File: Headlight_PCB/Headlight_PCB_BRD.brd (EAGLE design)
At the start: 100 x 80 mm, 7 parts, among them Q1 NTD3055L104G, Q2 NTD3055L104G

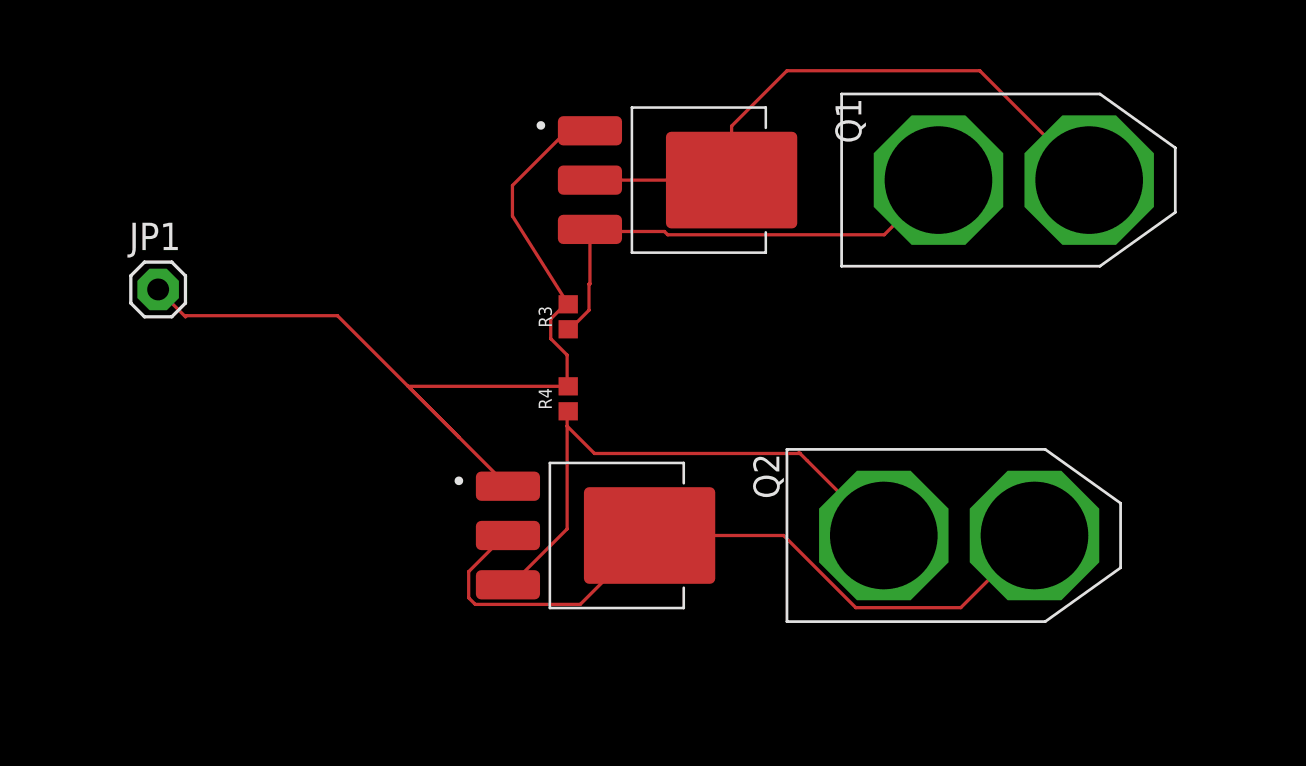
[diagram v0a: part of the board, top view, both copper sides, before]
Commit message: Updating\renaming Headlight_PCB files, adding pngs
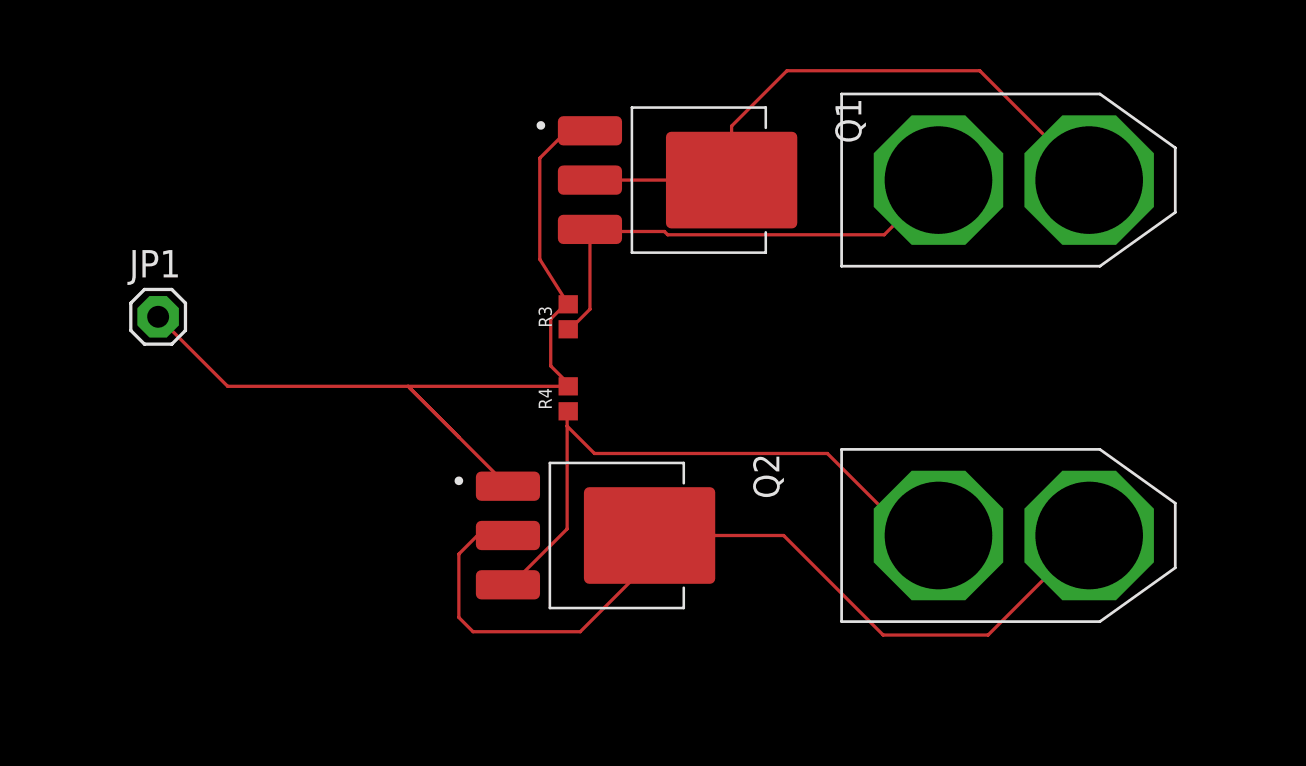
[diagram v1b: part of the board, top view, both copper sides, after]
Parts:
- moved U$2 2.54 mm to (40.6, 34.3)
- moved JP1 1.27 mm to (8.89, 44.5)
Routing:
- net N$4: track 34.2 -> 41.6 mm
- net N$5: track 26.4 -> 28.9 mm
- net N$7: track 46.3 -> 44.8 mm
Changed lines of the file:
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@@
 </autorouter>
 <elements>
-<element name="JP1" library="adafruit" package="1X01" value="" x="8.89" y="45.72" smashed="yes">
-<attribute name="NAME" x="7.5438" y="47.5488" size="1.27" layer="25" ratio="10"/>
-<attribute name="VALUE" x="7.62" y="42.545" size="1.27" layer="27"/>
+<element name="JP1" library="adafruit" package="1X01" value="" x="8.89" y="44.45" smashed="yes">
+<attribute name="NAME" x="7.5438" y="46.2788" size="1.27" layer="25" ratio="10"/>
+<attribute name="VALUE" x="7.62" y="41.275" size="1.27" layer="27"/>
 </element>
 <element name="Q1" library="Transistor" library_urn="urn:adsk.eagle:library:11396518" package="DPAK4" package3d_urn="urn:adsk.eagle:package:10893256/2" value="NTD3055L104G" x="33.02" y="50.8" smashed="yes" rot="R270">
@@
 </element>
 <element name="U$1" library="XT60" package="XT60" value="XT60" x="40.64" y="50.8" smashed="yes"/>
-<element name="U$2" library="XT60" package="XT60" value="XT60" x="38.1" y="34.29" smashed="yes"/>
+<element name="U$2" library="XT60" package="XT60" value="XT60" x="40.64" y="34.29" smashed="yes"/>
 <element name="R3" library="SparkFun-Resistors" package="0402" value="10k" x="27.94" y="44.45" smashed="yes" rot="R90">
 <attribute name="NAME" x="27.178" y="44.45" size="0.6096" layer="25" font="vector" ratio="20" rot="R90" align="bottom-center"/>
@@
 <contactref element="U$1" pad="+"/>
 <contactref element="Q1" pad="3"/>
-<wire x1="28.95" y1="45.98" x2="28.95" y2="48.51" width="0.1524" layer="1"/>
 <contactref element="R3" pad="1"/>
-<wire x1="28.9052" y1="44.7548" x2="28.0416" y2="43.8912" width="0.1524" layer="1"/>
-<wire x1="28.9052" y1="45.974" x2="28.9052" y2="44.7548" width="0.1524" layer="1"/>
+<wire x1="28.95" y1="44.7996" x2="28.0416" y2="43.8912" width="0.1524" layer="1"/>
+<wire x1="28.95" y1="48.51" x2="28.95" y2="44.7996" width="0.1524" layer="1"/>
 <wire x1="28.0416" y1="43.8912" x2="27.94" y2="43.87" width="0.1524" layer="1"/>
-<wire x1="28.9052" y1="45.974" x2="28.95" y2="45.98" width="0.1524" layer="1"/>
 <wire x1="32.4104" y1="48.4124" x2="29.0576" y2="48.4124" width="0.1524" layer="1"/>
 <wire x1="32.5628" y1="48.26" x2="32.4104" y2="48.4124" width="0.1524" layer="1"/>
@@
 <wire x1="22.86" y1="38.86" x2="25.14" y2="36.58" width="0.1524" layer="1"/>
 <wire x1="20.572" y1="41.148" x2="22.86" y2="38.86" width="0.1524" layer="1"/>
-<wire x1="10.16" y1="44.45" x2="8.89" y2="45.72" width="0.1524" layer="1"/>
 <contactref element="R3" pad="2"/>
 <contactref element="R4" pad="2"/>
-<wire x1="27.8892" y1="42.672" x2="27.8892" y2="41.3004" width="0.1524" layer="1"/>
-<wire x1="27.1272" y1="43.434" x2="27.8892" y2="42.672" width="0.1524" layer="1"/>
-<wire x1="27.1272" y1="44.3484" x2="27.1272" y2="43.434" width="0.1524" layer="1"/>
+<wire x1="27.8892" y1="41.402" x2="27.8892" y2="41.3004" width="0.1524" layer="1"/>
+<wire x1="27.1272" y1="42.164" x2="27.8892" y2="41.402" width="0.1524" layer="1"/>
+<wire x1="27.1272" y1="44.3484" x2="27.1272" y2="42.164" width="0.1524" layer="1"/>
 <wire x1="27.8892" y1="45.1104" x2="27.1272" y2="44.3484" width="0.1524" layer="1"/>
 <wire x1="27.8892" y1="41.3004" x2="27.94" y2="41.22" width="0.1524" layer="1"/>
 <wire x1="27.8892" y1="41.148" x2="27.94" y2="41.22" width="0.1524" layer="1"/>
-<wire x1="17.2212" y1="44.5008" x2="10.2108" y2="44.5008" width="0.1524" layer="1"/>
+<wire x1="20.502" y1="41.22" x2="12.12" y2="41.22" width="0.1524" layer="1"/>
+<wire x1="8.89" y1="44.45" x2="12.12" y2="41.22" width="0.1524" layer="1"/>
 <wire x1="22.86" y1="38.862" x2="20.502" y2="41.22" width="0.1524" layer="1"/>
-<wire x1="20.502" y1="41.22" x2="17.2212" y2="44.5008" width="0.1524" layer="1"/>
-<wire x1="10.2108" y1="44.5008" x2="10.16" y2="44.45" width="0.1524" layer="1"/>
 <wire x1="22.86" y1="38.862" x2="22.86" y2="38.86" width="0.1524" layer="1"/>
-<wire x1="25.3492" y1="49.1304" x2="25.3492" y2="50.55" width="0.1524" layer="1"/>
-<wire x1="25.3492" y1="49.1304" x2="27.8892" y2="45.1104" width="0.1524" layer="1"/>
+<wire x1="26.6192" y1="47.1204" x2="26.6192" y2="51.82" width="0.1524" layer="1"/>
+<wire x1="26.6192" y1="47.1204" x2="27.8892" y2="45.1104" width="0.1524" layer="1"/>
 <wire x1="27.8892" y1="45.1104" x2="27.94" y2="45.03" width="0.1524" layer="1"/>
 <wire x1="27.94" y1="41.22" x2="20.502" y2="41.22" width="0.1524" layer="1"/>
-<wire x1="25.3492" y1="50.55" x2="27.8892" y2="53.09" width="0.1524" layer="1"/>
+<wire x1="26.6192" y1="51.82" x2="27.8892" y2="53.09" width="0.1524" layer="1"/>
 <wire x1="27.8892" y1="53.09" x2="28.95" y2="53.09" width="0.1524" layer="1"/>
 </signal>
@@
 <contactref element="Q2" pad="4"/>
 <contactref element="U$2" pad="-"/>
-<wire x1="23.3172" y1="32.6136" x2="24.9936" y2="34.29" width="0.1524" layer="1"/>
-<wire x1="23.3172" y1="31.3944" x2="23.3172" y2="32.6136" width="0.1524" layer="1"/>
-<wire x1="23.622" y1="31.0896" x2="23.3172" y2="31.3944" width="0.1524" layer="1"/>
-<wire x1="28.4988" y1="31.0896" x2="23.622" y2="31.0896" width="0.1524" layer="1"/>
-<wire x1="31.6992" y1="34.29" x2="28.4988" y2="31.0896" width="0.1524" layer="1"/>
-<wire x1="24.9936" y1="34.29" x2="25.14" y2="34.29" width="0.1524" layer="1"/>
-<wire x1="31.6992" y1="34.29" x2="31.72" y2="34.29" width="0.1524" layer="1"/>
+<wire x1="22.86" y1="30.48" x2="23.5204" y2="29.8196" width="0.1524" layer="1"/>
+<wire x1="28.4988" y1="29.8196" x2="23.5204" y2="29.8196" width="0.1524" layer="1"/>
+<wire x1="31.72" y1="34.29" x2="31.72" y2="33.0408" width="0.1524" layer="1"/>
+<wire x1="31.72" y1="33.0408" x2="28.4988" y2="29.8196" width="0.1524" layer="1"/>
+<wire x1="25.14" y1="34.29" x2="23.7236" y2="34.29" width="0.1524" layer="1"/>
 <wire x1="37.9476" y1="34.29" x2="31.72" y2="34.29" width="0.1524" layer="1"/>
-<wire x1="41.3004" y1="30.9372" x2="37.9476" y2="34.29" width="0.1524" layer="1"/>
-<wire x1="46.1772" y1="30.9372" x2="41.3004" y2="30.9372" width="0.1524" layer="1"/>
-<wire x1="49.53" y1="34.29" x2="46.1772" y2="30.9372" width="0.1524" layer="1"/>
-<wire x1="49.53" y1="34.29" x2="49.6" y2="34.29" width="0.1524" layer="1"/>
+<wire x1="42.5704" y1="29.6672" x2="37.9476" y2="34.29" width="0.1524" layer="1"/>
+<wire x1="47.4472" y1="29.6672" x2="42.5704" y2="29.6672" width="0.1524" layer="1"/>
+<wire x1="52.07" y1="34.29" x2="47.4472" y2="29.6672" width="0.1524" layer="1"/>
+<wire x1="52.07" y1="34.29" x2="52.14" y2="34.29" width="0.1524" layer="1"/>
+<wire x1="22.86" y1="33.4264" x2="22.86" y2="30.48" width="0.1524" layer="1"/>
+<wire x1="23.7236" y1="34.29" x2="22.86" y2="33.4264" width="0.1524" layer="1"/>
 </signal>
 <signal name="N$5">
@@
 <wire x1="27.8892" y1="39.9288" x2="27.94" y2="40.06" width="0.1524" layer="1"/>
 <wire x1="25.146" y1="31.8516" x2="25.14" y2="32" width="0.1524" layer="1"/>
-<wire x1="42.5196" y1="34.29" x2="39.0398" y2="37.7698" width="0.1524" layer="1"/>
-<wire x1="38.7096" y1="38.1" x2="38.6588" y2="38.1508" width="0.1524" layer="1"/>
-<wire x1="42.5196" y1="34.29" x2="42.6" y2="34.29" width="0.1524" layer="1"/>
-<wire x1="39.0398" y1="37.7698" x2="38.7096" y2="38.1" width="0.1524" layer="1"/>
+<wire x1="43.7896" y1="34.29" x2="39.9796" y2="38.1" width="0.1524" layer="1"/>
+<wire x1="43.7896" y1="34.29" x2="45.14" y2="34.29" width="0.1524" layer="1"/>
 <wire x1="29.1592" y1="38.1" x2="27.8892" y2="39.37" width="0.1524" layer="1"/>
-<wire x1="38.7096" y1="38.1" x2="29.1592" y2="38.1" width="0.1524" layer="1"/>
+<wire x1="39.9796" y1="38.1" x2="29.1592" y2="38.1" width="0.1524" layer="1"/>
 </signal>
 <signal name="N$3">
